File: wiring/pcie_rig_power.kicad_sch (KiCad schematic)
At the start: 13 parts, among them J1 XT60E-M, J2a post +, J2b post -, J3 XT60E-F RISER, J4 XT60E-F CARD, J5a post +, J5b post -, J6 PROBE GND, M1 PZEM-031, SW1 rocker

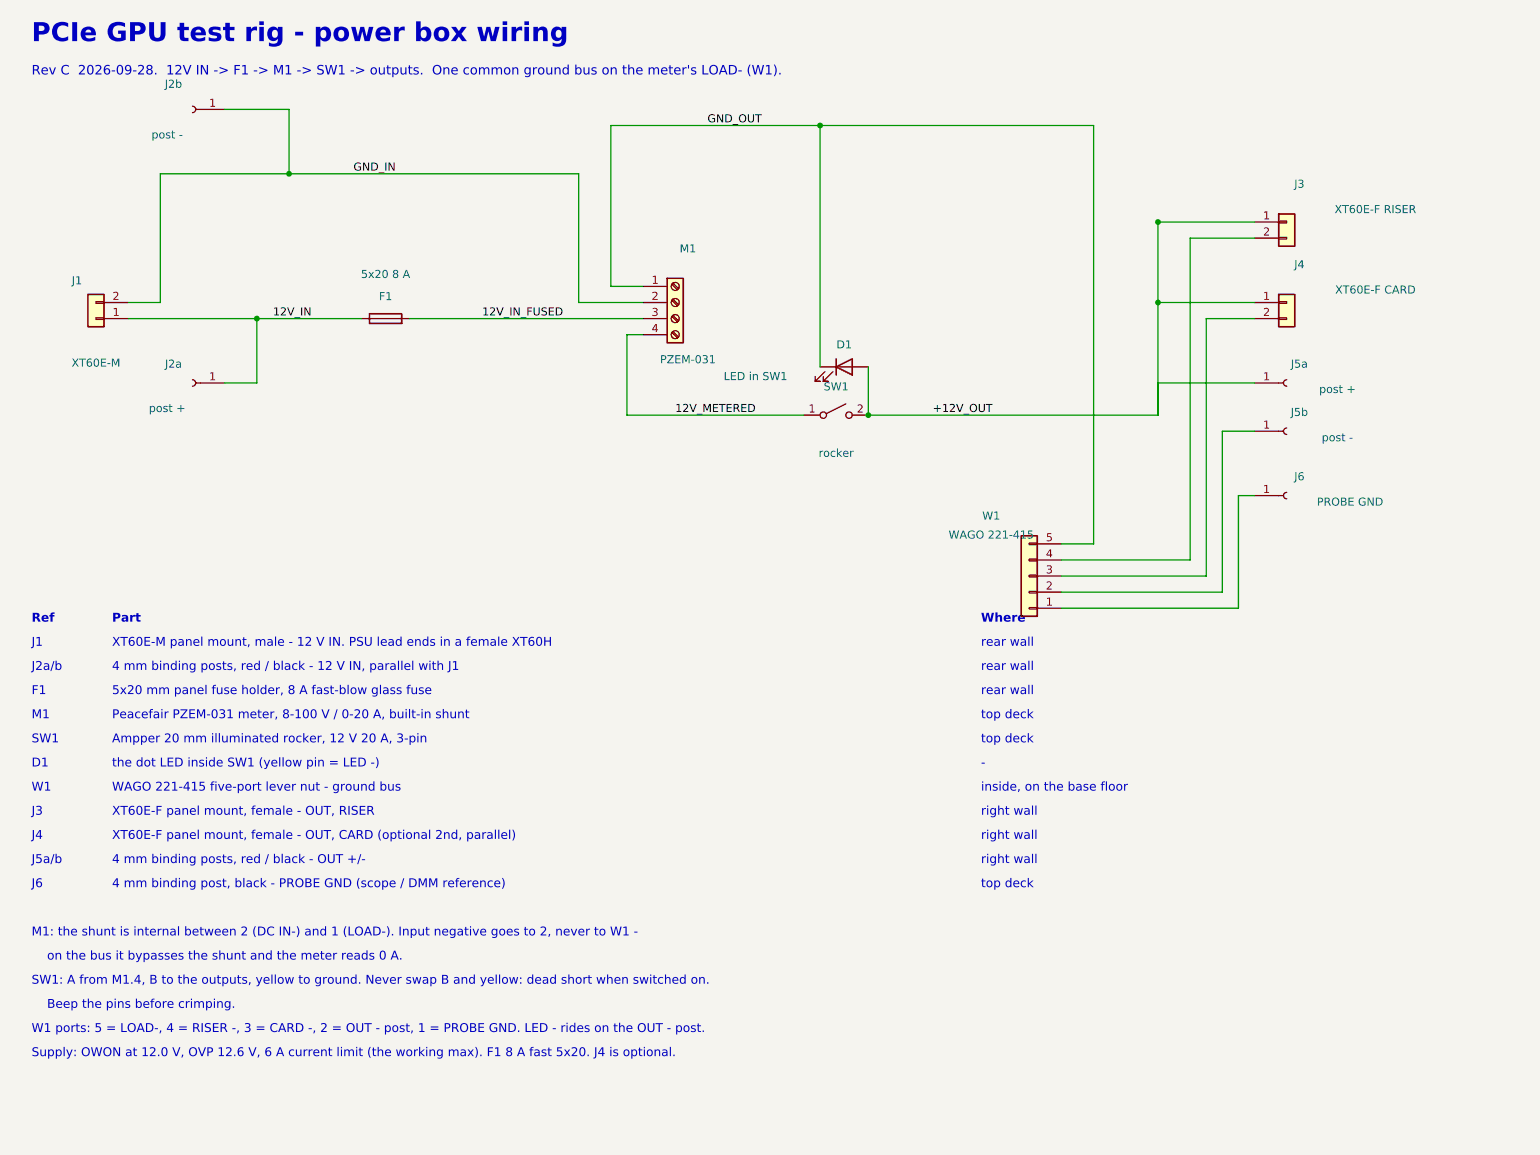
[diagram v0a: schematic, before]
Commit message: feat(wiring): rev D — WAGO 221 lever nuts join the input pair (W3/W4), the switched + bus (W2) and the ground bus (W1); no two wires on one terminal
Signed-off-by: Aaron Cupp <mrcupp@mrcupp.com>
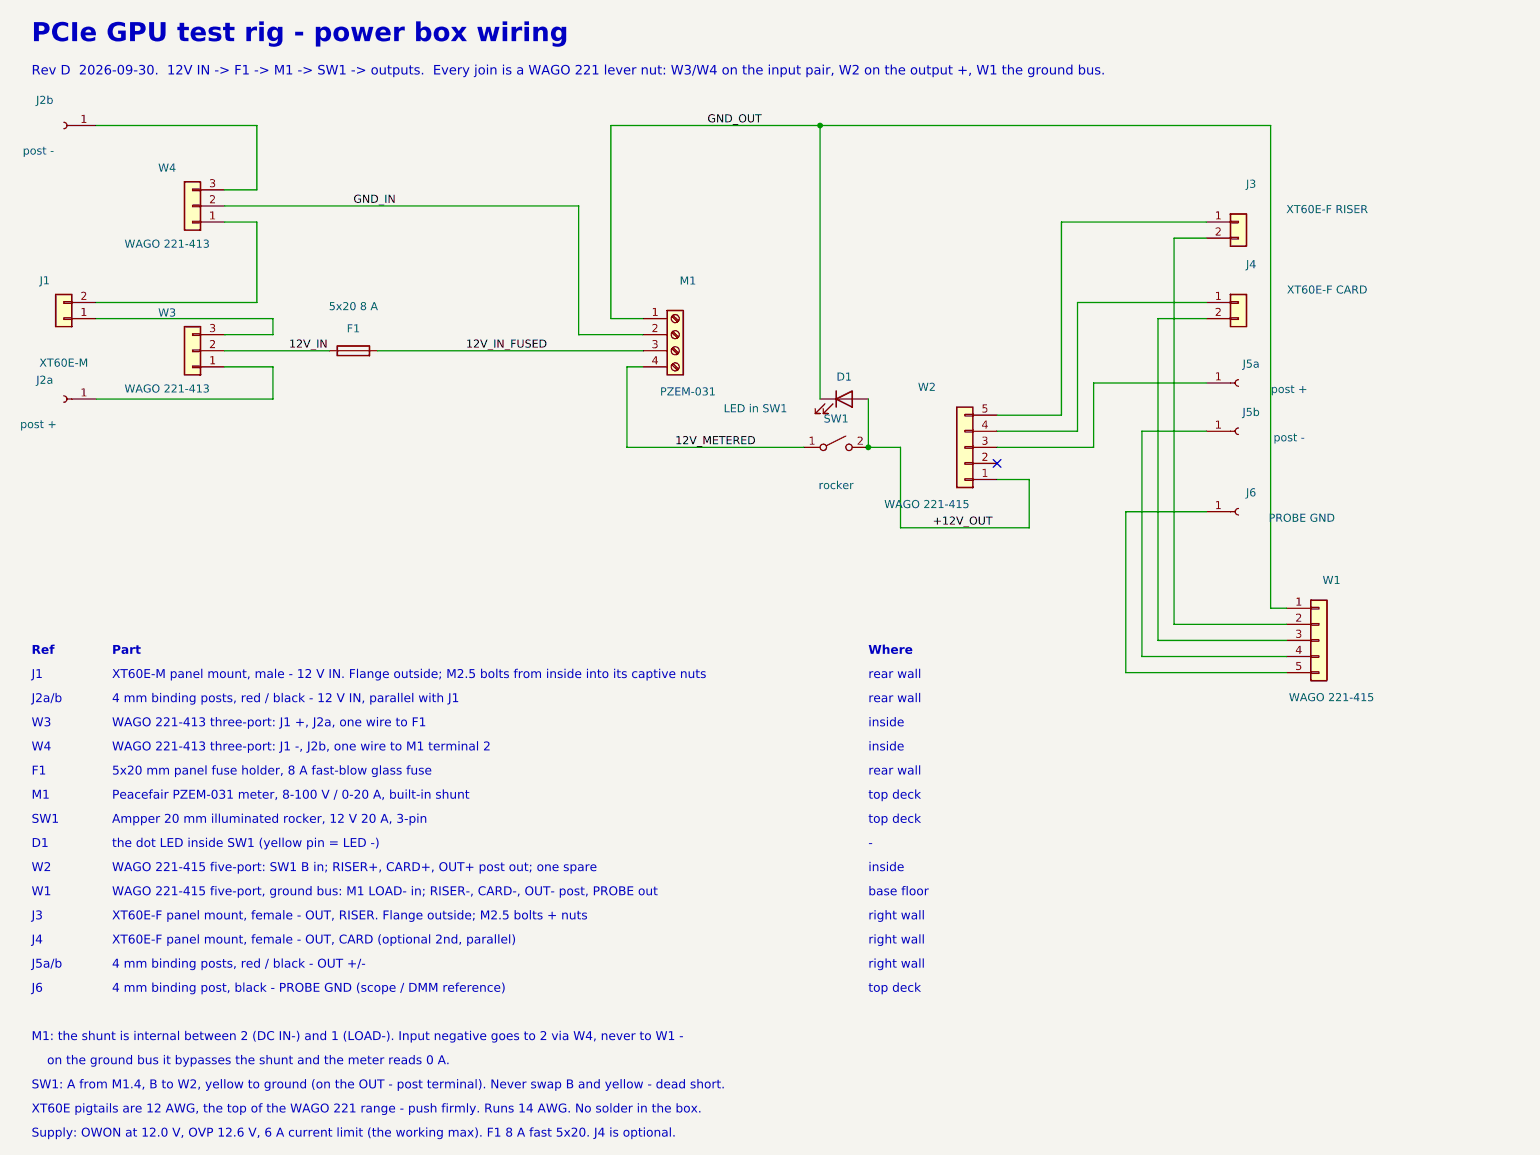
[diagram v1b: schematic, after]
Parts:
- removed M1: PZEM-031, symbol Connector:Screw_Terminal_01x04
- added J4: XT60E-F CARD, symbol Connector_Generic:Conn_01x02
- added J6: PROBE GND, symbol Connector:Conn_01x01_Socket
- added W2: WAGO 221-415, symbol Connector_Generic:Conn_01x05
- added W3: WAGO 221-413, symbol Connector_Generic:Conn_01x03
- M1: renamed from J6; value PROBE GND -> PZEM-031; symbol Connector:Conn_01x01_Socket -> Connector:Screw_Terminal_01x04
- W4: renamed from J4; value XT60E-F CARD -> WAGO 221-413; symbol Connector_Generic:Conn_01x02 -> Connector_Generic:Conn_01x03
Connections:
- net +12V_OUT: now also W2.1 (Pin_1); no longer J3.1 (Pin_1), J5a.1 (Pin_1), W4.1 (Pin_1)
- net 12V_IN: now also W3.2 (Pin_2); no longer J1.1 (Pin_1), J2a.1 (Pin_1)
- net 12V_IN_FUSED: now also M1.3 (Pin_3)
- net 12V_METERED: now also M1.4 (Pin_4)
- net GND_IN: now also M1.2 (Pin_2), W4.2 (Pin_2); no longer J1.2 (Pin_2), J2b.1 (Pin_1)
- net GND_OUT: now also M1.1 (Pin_1), W1.1 (Pin_1); no longer W1.5 (Pin_5)
- net at W1.2 (Pin_2): now also J3.2 (Pin_2); no longer J5b.1 (Pin_1)
- net at W1.3 (Pin_3): now also J4.2 (Pin_2); no longer W4.2 (Pin_2)
- net at W1.4 (Pin_4): now also J5b.1 (Pin_1); no longer J3.2 (Pin_2)
- new net: J1.1 (Pin_1), W3.3 (Pin_3)
- new net: J1.2 (Pin_2), W4.1 (Pin_1)
- new net: J2a.1 (Pin_1), W3.1 (Pin_1)
- new net: J2b.1 (Pin_1), W4.3 (Pin_3)
- new net: J5a.1 (Pin_1), W2.3 (Pin_3)
- new net: J4.1 (Pin_1), W2.4 (Pin_4)
- new net: J3.1 (Pin_1), W2.5 (Pin_5)
- new net: J6.1 (Pin_1), W1.5 (Pin_5)
- no-connect marks 0 -> 1
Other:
- note added: "M1: the shunt is internal between 2 (DC IN-) and 1 (LOAD-). Input negative goes to 2 via W4, never to W1 -"
- note added: "Rev D 2026-09-30. 12V IN -> F1 -> M1 -> SW1 -> outputs. Every join is a WAGO 221 lever nut: W3/W4 on the input pair, W2 on the output +, W1 the ground bus."
- note added: "SW1: A from M1.4, B to W2, yellow to ground (on the OUT - post terminal). Never swap B and yellow - dead short."
- note added: "W2"
- note added: "W3"
- note added: "W4"
- note added: "WAGO 221-413 three-port: J1 +, J2a, one wire to F1"
- note added: "WAGO 221-413 three-port: J1 -, J2b, one wire to M1 terminal 2"
- note added: "WAGO 221-415 five-port, ground bus: M1 LOAD- in; RISER-, CARD-, OUT- post, PROBE out"
- note added: "WAGO 221-415 five-port: SW1 B in; RISER+, CARD+, OUT+ post out; one spare"
- note added: "XT60E pigtails are 12 AWG, the top of the WAGO 221 range - push firmly. Runs 14 AWG. No solder in the box."
- note added: "XT60E-F panel mount, female - OUT, RISER. Flange outside; M2.5 bolts + nuts"
- note added: "XT60E-M panel mount, male - 12 V IN. Flange outside; M2.5 bolts from inside into its captive nuts"
- note added: "base floor"
- note added: "inside"
- note added: "on the ground bus it bypasses the shunt and the meter reads 0 A."
- note removed: "Beep the pins before crimping."
- note removed: "M1: the shunt is internal between 2 (DC IN-) and 1 (LOAD-). Input negative goes to 2, never to W1 -"
- note removed: "Rev C 2026-09-28. 12V IN -> F1 -> M1 -> SW1 -> outputs. One common ground bus on the meter's LOAD- (W1)."
- note removed: "SW1: A from M1.4, B to the outputs, yellow to ground. Never swap B and yellow: dead short when switched on."
- note removed: "W1 ports: 5 = LOAD-, 4 = RISER -, 3 = CARD -, 2 = OUT - post, 1 = PROBE GND. LED - rides on the OUT - post."
- note removed: "WAGO 221-415 five-port lever nut - ground bus"
- note removed: "XT60E-F panel mount, female - OUT, RISER"
- note removed: "XT60E-M panel mount, male - 12 V IN. PSU lead ends in a female XT60H"
- note removed: "inside, on the base floor"
- note removed: "on the bus it bypasses the shunt and the meter reads 0 A."

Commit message: docs: split into BOM.md, BUILD.md and a reference WIRING.md; KiCad-exported BOM checked in CI; posts renumbered J2/J7/J5/J8
Signed-off-by: Aaron Cupp <mrcupp@mrcupp.com>
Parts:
- renumbered J2a to J2, J5a to J5, J2b to J7, J5b to J8
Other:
- note added: "J2 J7"
- note added: "J5 J8"
- note added: "WAGO 221-413 three-port: J1 +, J2, one wire to F1"
- note added: "WAGO 221-413 three-port: J1 -, J7, one wire to M1 terminal 2"
- note removed: "J2a/b"
- note removed: "J5a/b"
- note removed: "WAGO 221-413 three-port: J1 +, J2a, one wire to F1"
- note removed: "WAGO 221-413 three-port: J1 -, J2b, one wire to M1 terminal 2"
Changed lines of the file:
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@@
 	)
 	(text
-		"J2a/b"
+		"J2 J7"
 		(exclude_from_sim no)
 		(at 20.32 127.0 0)
@@
 	)
 	(text
-		"WAGO 221-413 three-port: J1 +, J2a, one wire to F1"
+		"WAGO 221-413 three-port: J1 +, J2, one wire to F1"
 		(exclude_from_sim no)
 		(at 33.019999999999996 130.81 0)
@@
 	)
 	(text
-		"WAGO 221-413 three-port: J1 -, J2b, one wire to M1 terminal 2"
+		"WAGO 221-413 three-port: J1 -, J7, one wire to M1 terminal 2"
 		(exclude_from_sim no)
 		(at 33.019999999999996 134.62 0)
@@
 	)
 	(text
-		"J5a/b"
+		"J5 J8"
 		(exclude_from_sim no)
 		(at 20.32 168.91 0)
@@
 		(on_board yes)
 		(dnp no)
-		(property "Reference" "J2a" (at 22.4 75.74 0) (effects (font (size 1.27 1.27))))
+		(property "Reference" "J2" (at 22.4 75.74 0) (effects (font (size 1.27 1.27))))
 		(property "Value" "post +" (at 21.4 82.74 0) (effects (font (size 1.27 1.27))))
 		(property "Footprint" "" (at 25.4 78.74 0) (effects (font (size 1.27 1.27)) (hide yes)))
@@
 		(pin "1")
 		(instances
-			(project "pcie_rig_power" (path "/6b2f0c1e-1000-4000-8000-000000000000" (reference "J2a") (unit 1)))
+			(project "pcie_rig_power" (path "/6b2f0c1e-1000-4000-8000-000000000000" (reference "J2") (unit 1)))
 		)
 	)
@@
 		(on_board yes)
 		(dnp no)
-		(property "Reference" "J2b" (at 22.4 31.56 0) (effects (font (size 1.27 1.27))))
+		(property "Reference" "J7" (at 22.4 31.56 0) (effects (font (size 1.27 1.27))))
 		(property "Value" "post -" (at 21.4 39.56 0) (effects (font (size 1.27 1.27))))
 		(property "Footprint" "" (at 25.4 35.56 0) (effects (font (size 1.27 1.27)) (hide yes)))
@@
 		(pin "1")
 		(instances
-			(project "pcie_rig_power" (path "/6b2f0c1e-1000-4000-8000-000000000000" (reference "J2b") (unit 1)))
+			(project "pcie_rig_power" (path "/6b2f0c1e-1000-4000-8000-000000000000" (reference "J7") (unit 1)))
 		)
 	)
@@
 		(on_board yes)
 		(dnp no)
-		(property "Reference" "J5a" (at 212.82 73.2 0) (effects (font (size 1.27 1.27))))
+		(property "Reference" "J5" (at 212.82 73.2 0) (effects (font (size 1.27 1.27))))
 		(property "Value" "post +" (at 218.82 77.2 0) (effects (font (size 1.27 1.27))))
 		(property "Footprint" "" (at 210.82 76.2 0) (effects (font (size 1.27 1.27)) (hide yes)))
@@
 		(pin "1")
 		(instances
-			(project "pcie_rig_power" (path "/6b2f0c1e-1000-4000-8000-000000000000" (reference "J5a") (unit 1)))
+			(project "pcie_rig_power" (path "/6b2f0c1e-1000-4000-8000-000000000000" (reference "J5") (unit 1)))
 		)
 	)
@@
 		(on_board yes)
 		(dnp no)
-		(property "Reference" "J5b" (at 212.82 80.82 0) (effects (font (size 1.27 1.27))))
+		(property "Reference" "J8" (at 212.82 80.82 0) (effects (font (size 1.27 1.27))))
 		(property "Value" "post -" (at 218.82 84.82 0) (effects (font (size 1.27 1.27))))
 		(property "Footprint" "" (at 210.82 83.82 0) (effects (font (size 1.27 1.27)) (hide yes)))
@@
 		(pin "1")
 		(instances
-			(project "pcie_rig_power" (path "/6b2f0c1e-1000-4000-8000-000000000000" (reference "J5b") (unit 1)))
-		)
-	)
+			(project "pcie_rig_power" (path "/6b2f0c1e-1000-4000-8000-000000000000" (reference "J8") (unit 1)))
+		)
+	)
